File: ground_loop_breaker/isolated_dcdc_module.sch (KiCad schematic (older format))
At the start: 18 parts, among them J1 Conn_01x02_Male, J2 Conn_01x02_Male, J3 Conn_Coaxial

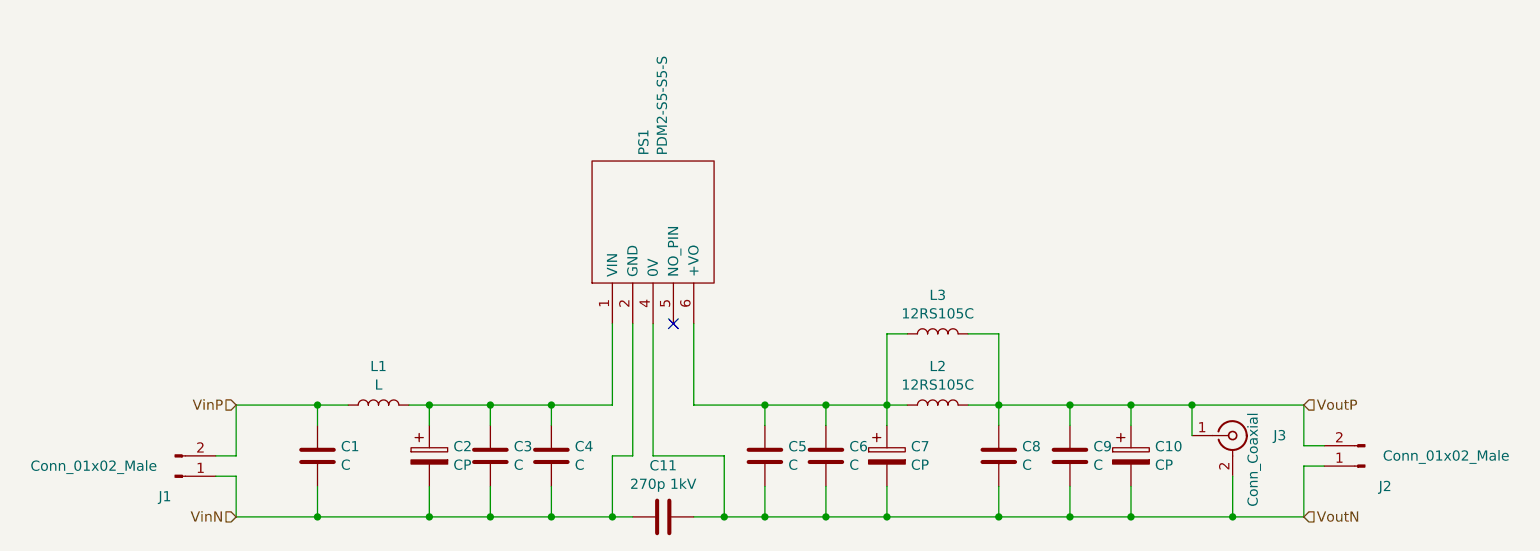
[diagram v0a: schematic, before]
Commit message: ground loop breaker fin
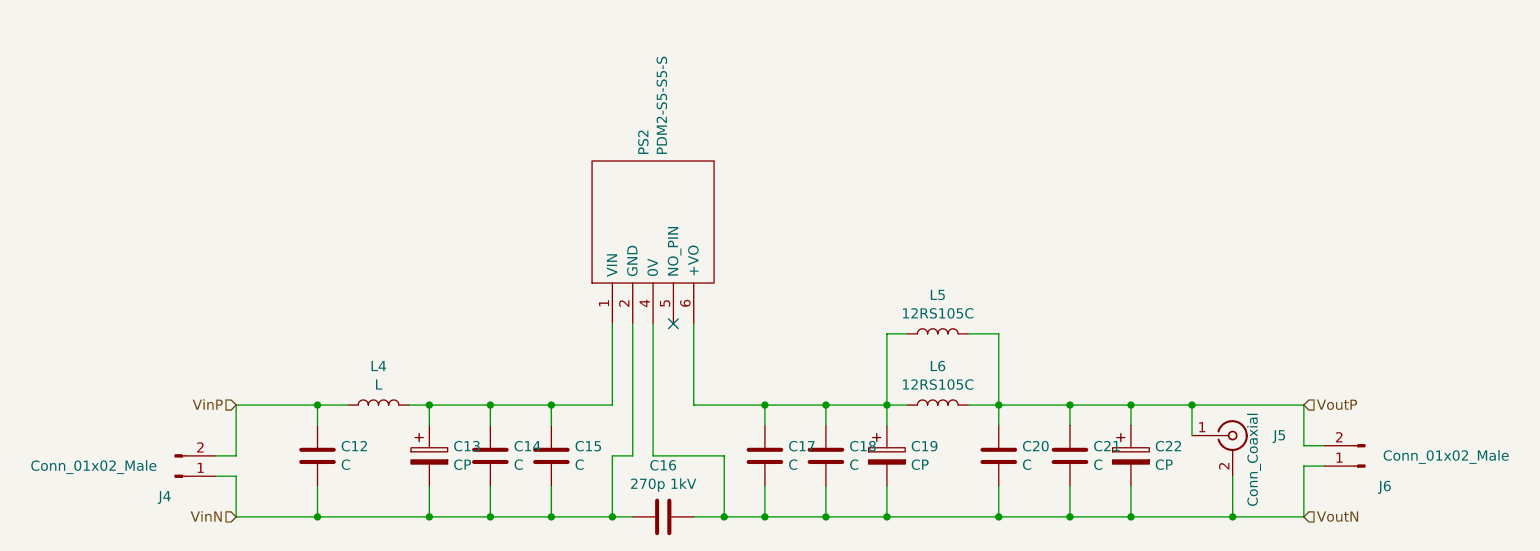
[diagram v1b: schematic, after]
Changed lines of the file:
@@
 $Descr A4 11693 8268
 encoding utf-8
-Sheet 2 5
+Sheet 4 5
 Title ""
 Date ""
@@
 AR Path="/613586DE/6135B5DE" Ref="C15"  Part="1"
 AR Path="/61358712/6135B5DE" Ref="C37"  Part="1"
-F 0 "C4" H 4165 3446 50  0000 L CNN
+F 0 "C15" H 4165 3446 50  0000 L CNN
 F 1 "C" H 4165 3355 50  0000 L CNN
 F 2 "SamacSys_Parts:C_1206_0805_dual" H 4088 3250 50  0001 C CNN
@@
 AR Path="/613586DE/6135B5E4" Ref="C14"  Part="1"
 AR Path="/61358712/6135B5E4" Ref="C36"  Part="1"
-F 0 "C3" H 3865 3446 50  0000 L CNN
+F 0 "C14" H 3865 3446 50  0000 L CNN
 F 1 "C" H 3865 3355 50  0000 L CNN
 F 2 "Capacitor_SMD:C_1206_3216Metric_Pad1.42x1.75mm_HandSolder" H 3788 3250 50  0001 C CNN
@@
 AR Path="/613586DE/6135B5F2" Ref="C13"  Part="1"
 AR Path="/61358712/6135B5F2" Ref="C35"  Part="1"
-F 0 "C2" H 3568 3446 50  0000 L CNN
+F 0 "C13" H 3568 3446 50  0000 L CNN
 F 1 "CP" H 3568 3355 50  0000 L CNN
 F 2 "SamacSys_Parts:CP_Radial_D8_P3.5_2.5" H 3488 3250 50  0001 C CNN
@@
 AR Path="/613586DE/6135B603" Ref="C12"  Part="1"
 AR Path="/61358712/6135B603" Ref="C34"  Part="1"
-F 0 "C1" H 3015 3446 50  0000 L CNN
+F 0 "C12" H 3015 3446 50  0000 L CNN
 F 1 "C" H 3015 3355 50  0000 L CNN
 F 2 "Capacitor_SMD:C_1206_3216Metric_Pad1.42x1.75mm_HandSolder" H 2938 3250 50  0001 C CNN
@@
 AR Path="/613586DE/6135B609" Ref="L4"  Part="1"
 AR Path="/61358712/6135B609" Ref="L10"  Part="1"
-F 0 "L1" V 3390 3150 50  0000 C CNN
+F 0 "L4" V 3390 3150 50  0000 C CNN
 F 1 "L" V 3299 3150 50  0000 C CNN
 F 2 "Inductor_SMD:L_Bourns-SRN4018" H 3200 3150 50  0001 C CNN
@@
 AR Path="/613586DE/61362EDF" Ref="C18"  Part="1"
 AR Path="/61358712/61362EDF" Ref="C40"  Part="1"
-F 0 "C6" H 5515 3446 50  0000 L CNN
+F 0 "C18" H 5515 3446 50  0000 L CNN
 F 1 "C" H 5515 3355 50  0000 L CNN
 F 2 "Capacitor_SMD:C_1206_3216Metric_Pad1.42x1.75mm_HandSolder" H 5438 3250 50  0001 C CNN
@@
 AR Path="/613586DE/61362EFB" Ref="C20"  Part="1"
 AR Path="/61358712/61362EFB" Ref="C42"  Part="1"
-F 0 "C8" H 6365 3446 50  0000 L CNN
+F 0 "C20" H 6365 3446 50  0000 L CNN
 F 1 "C" H 6365 3355 50  0000 L CNN
 F 2 "Capacitor_SMD:C_1206_3216Metric_Pad1.42x1.75mm_HandSolder" H 6288 3250 50  0001 C CNN
@@
 AR Path="/613586DE/61362F01" Ref="L6"  Part="1"
 AR Path="/61358712/61362F01" Ref="L12"  Part="1"
-F 0 "L2" V 6140 3150 50  0000 C CNN
+F 0 "L6" V 6140 3150 50  0000 C CNN
 F 1 "12RS105C" V 6049 3150 50  0000 C CNN
 F 2 "Inductor_THT:L_Radial_D10.5mm_P4.00x5.00mm_Murata_1200RS" H 5950 3150 50  0001 C CNN
@@
 AR Path="/613586DE/61365071" Ref="C17"  Part="1"
 AR Path="/61358712/61365071" Ref="C39"  Part="1"
-F 0 "C5" H 5215 3446 50  0000 L CNN
+F 0 "C17" H 5215 3446 50  0000 L CNN
 F 1 "C" H 5215 3355 50  0000 L CNN
 F 2 "SamacSys_Parts:C_1206_0805_dual" H 5138 3250 50  0001 C CNN
@@
 AR Path="/613586DE/613683EF" Ref="C21"  Part="1"
 AR Path="/61358712/613683EF" Ref="C43"  Part="1"
-F 0 "C9" H 6715 3446 50  0000 L CNN
+F 0 "C21" H 6715 3446 50  0000 L CNN
 F 1 "C" H 6715 3355 50  0000 L CNN
 F 2 "Capacitor_SMD:C_1206_3216Metric_Pad1.42x1.75mm_HandSolder" H 6638 3250 50  0001 C CNN
@@
 AR Path="/613586DE/613683F5" Ref="C22"  Part="1"
 AR Path="/61358712/613683F5" Ref="C44"  Part="1"
-F 0 "C10" H 7018 3446 50  0000 L CNN
+F 0 "C22" H 7018 3446 50  0000 L CNN
 F 1 "CP" H 7018 3355 50  0000 L CNN
 F 2 "SamacSys_Parts:CP_Radial_D10.0mm_P3.5_5" H 6938 3250 50  0001 C CNN
@@
 AR Path="/613586DE/6136C0C2" Ref="C19"  Part="1"
 AR Path="/61358712/6136C0C2" Ref="C41"  Part="1"
-F 0 "C7" H 5818 3446 50  0000 L CNN
+F 0 "C19" H 5818 3446 50  0000 L CNN
 F 1 "CP" H 5818 3355 50  0000 L CNN
 F 2 "SamacSys_Parts:CP_Radial_D8_P3.5_2.5" H 5738 3250 50  0001 C CNN
@@
 AR Path="/613586DE/6135AA09" Ref="J4"  Part="1"
 AR Path="/61358712/6135AA09" Ref="J10"  Part="1"
-F 0 "J1" H 2150 3600 50  0000 C CNN
+F 0 "J4" H 2150 3600 50  0000 C CNN
 F 1 "Conn_01x02_Male" H 1800 3450 50  0000 C CNN
 F 2 "Connector_PinHeader_2.54mm:PinHeader_1x02_P2.54mm_Vertical" H 2200 3500 50  0001 C CNN
@@
 AR Path="/613586DE/6135E9D7" Ref="J6"  Part="1"
 AR Path="/61358712/6135E9D7" Ref="J12"  Part="1"
-F 0 "J2" H 7950 3550 50  0000 C CNN
+F 0 "J6" H 7950 3550 50  0000 C CNN
 F 1 "Conn_01x02_Male" H 7650 3400 50  0000 C CNN
 F 2 "Connector_PinHeader_2.54mm:PinHeader_1x02_P2.54mm_Vertical" H 8050 3450 50  0001 C CNN
@@
 AR Path="/613586DE/613639F2" Ref="PS2"  Part="1"
 AR Path="/61358712/613639F2" Ref="PS4"  Part="1"
-F 0 "PS1" H 5178 2596 50  0000 L CNN
+F 0 "PS2" H 5178 2596 50  0000 L CNN
 F 1 "PDM2-S5-S5-S" H 5178 2505 50  0000 L CNN
 F 2 "PDM2S5S5S" H 5200 2850 50  0001 L CNN
@@
 AR Path="/613586DE/6137BF49" Ref="L5"  Part="1"
 AR Path="/61358712/6137BF49" Ref="L11"  Part="1"
-F 0 "L3" V 6140 2800 50  0000 C CNN
+F 0 "L5" V 6140 2800 50  0000 C CNN
 F 1 "12RS105C" V 6049 2800 50  0000 C CNN
 F 2 "Inductor_THT:L_Radial_D10.0mm_P5.00mm_Fastron_07P" H 5950 2800 50  0001 C CNN
@@
 AR Path="/613586DE/61387E06" Ref="C16"  Part="1"
 AR Path="/61358712/61387E06" Ref="C38"  Part="1"
-F 0 "C11" V 4348 3700 50  0000 C CNN
+F 0 "C16" V 4348 3700 50  0000 C CNN
 F 1 "270p 1kV" V 4439 3700 50  0000 C CNN
 F 2 "Capacitor_SMD:C_1206_3216Metric_Pad1.42x1.75mm_HandSolder" H 4638 3550 50  0001 C CNN
@@
 AR Path="/613586DE/61392101" Ref="J5"  Part="1"
 AR Path="/61358712/61392101" Ref="J11"  Part="1"
-F 0 "J3" H 7600 3300 50  0000 L CNN
+F 0 "J5" H 7600 3300 50  0000 L CNN
 F 1 "Conn_Coaxial" V 7500 2950 50  0000 L CNN
 F 2 "Connector_Coaxial:U.FL_Hirose_U.FL-R-SMT-1_Vertical" H 7400 3300 50  0001 C CNN

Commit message: Relay array board; Last checkup; Gerberfile updates
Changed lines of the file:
@@
 $Descr A4 11693 8268
 encoding utf-8
-Sheet 4 5
+Sheet 4 6
 Title ""
 Date ""
@@
 AR Path="/613586DE/6135B5DE" Ref="C15"  Part="1"
 AR Path="/61358712/6135B5DE" Ref="C37"  Part="1"
-F 0 "C15" H 4165 3446 50  0000 L CNN
+F 0 "C37" H 4165 3446 50  0000 L CNN
 F 1 "C" H 4165 3355 50  0000 L CNN
 F 2 "SamacSys_Parts:C_1206_0805_dual" H 4088 3250 50  0001 C CNN
@@
 AR Path="/613586DE/6135B5E4" Ref="C14"  Part="1"
 AR Path="/61358712/6135B5E4" Ref="C36"  Part="1"
-F 0 "C14" H 3865 3446 50  0000 L CNN
+F 0 "C36" H 3865 3446 50  0000 L CNN
 F 1 "C" H 3865 3355 50  0000 L CNN
 F 2 "Capacitor_SMD:C_1206_3216Metric_Pad1.42x1.75mm_HandSolder" H 3788 3250 50  0001 C CNN
@@
 AR Path="/613586DE/6135B5F2" Ref="C13"  Part="1"
 AR Path="/61358712/6135B5F2" Ref="C35"  Part="1"
-F 0 "C13" H 3568 3446 50  0000 L CNN
+F 0 "C35" H 3568 3446 50  0000 L CNN
 F 1 "CP" H 3568 3355 50  0000 L CNN
 F 2 "SamacSys_Parts:CP_Radial_D8_P3.5_2.5" H 3488 3250 50  0001 C CNN
@@
 AR Path="/613586DE/6135B603" Ref="C12"  Part="1"
 AR Path="/61358712/6135B603" Ref="C34"  Part="1"
-F 0 "C12" H 3015 3446 50  0000 L CNN
+F 0 "C34" H 3015 3446 50  0000 L CNN
 F 1 "C" H 3015 3355 50  0000 L CNN
 F 2 "Capacitor_SMD:C_1206_3216Metric_Pad1.42x1.75mm_HandSolder" H 2938 3250 50  0001 C CNN
@@
 AR Path="/613586DE/6135B609" Ref="L4"  Part="1"
 AR Path="/61358712/6135B609" Ref="L10"  Part="1"
-F 0 "L4" V 3390 3150 50  0000 C CNN
+F 0 "L10" V 3390 3150 50  0000 C CNN
 F 1 "L" V 3299 3150 50  0000 C CNN
 F 2 "Inductor_SMD:L_Bourns-SRN4018" H 3200 3150 50  0001 C CNN
@@
 AR Path="/613586DE/61362EDF" Ref="C18"  Part="1"
 AR Path="/61358712/61362EDF" Ref="C40"  Part="1"
-F 0 "C18" H 5515 3446 50  0000 L CNN
+F 0 "C40" H 5515 3446 50  0000 L CNN
 F 1 "C" H 5515 3355 50  0000 L CNN
 F 2 "Capacitor_SMD:C_1206_3216Metric_Pad1.42x1.75mm_HandSolder" H 5438 3250 50  0001 C CNN
@@
 AR Path="/613586DE/61362EFB" Ref="C20"  Part="1"
 AR Path="/61358712/61362EFB" Ref="C42"  Part="1"
-F 0 "C20" H 6365 3446 50  0000 L CNN
+F 0 "C42" H 6365 3446 50  0000 L CNN
 F 1 "C" H 6365 3355 50  0000 L CNN
 F 2 "Capacitor_SMD:C_1206_3216Metric_Pad1.42x1.75mm_HandSolder" H 6288 3250 50  0001 C CNN
@@
 AR Path="/613586DE/61362F01" Ref="L6"  Part="1"
 AR Path="/61358712/61362F01" Ref="L12"  Part="1"
-F 0 "L6" V 6140 3150 50  0000 C CNN
+F 0 "L12" V 6140 3150 50  0000 C CNN
 F 1 "12RS105C" V 6049 3150 50  0000 C CNN
 F 2 "Inductor_THT:L_Radial_D10.5mm_P4.00x5.00mm_Murata_1200RS" H 5950 3150 50  0001 C CNN
@@
 AR Path="/613586DE/61365071" Ref="C17"  Part="1"
 AR Path="/61358712/61365071" Ref="C39"  Part="1"
-F 0 "C17" H 5215 3446 50  0000 L CNN
+F 0 "C39" H 5215 3446 50  0000 L CNN
 F 1 "C" H 5215 3355 50  0000 L CNN
 F 2 "SamacSys_Parts:C_1206_0805_dual" H 5138 3250 50  0001 C CNN
@@
 AR Path="/613586DE/613683EF" Ref="C21"  Part="1"
 AR Path="/61358712/613683EF" Ref="C43"  Part="1"
-F 0 "C21" H 6715 3446 50  0000 L CNN
+F 0 "C43" H 6715 3446 50  0000 L CNN
 F 1 "C" H 6715 3355 50  0000 L CNN
 F 2 "Capacitor_SMD:C_1206_3216Metric_Pad1.42x1.75mm_HandSolder" H 6638 3250 50  0001 C CNN
@@
 AR Path="/613586DE/613683F5" Ref="C22"  Part="1"
 AR Path="/61358712/613683F5" Ref="C44"  Part="1"
-F 0 "C22" H 7018 3446 50  0000 L CNN
+F 0 "C44" H 7018 3446 50  0000 L CNN
 F 1 "CP" H 7018 3355 50  0000 L CNN
 F 2 "SamacSys_Parts:CP_Radial_D10.0mm_P3.5_5" H 6938 3250 50  0001 C CNN
@@
 AR Path="/613586DE/6136C0C2" Ref="C19"  Part="1"
 AR Path="/61358712/6136C0C2" Ref="C41"  Part="1"
-F 0 "C19" H 5818 3446 50  0000 L CNN
+F 0 "C41" H 5818 3446 50  0000 L CNN
 F 1 "CP" H 5818 3355 50  0000 L CNN
 F 2 "SamacSys_Parts:CP_Radial_D8_P3.5_2.5" H 5738 3250 50  0001 C CNN
@@
 AR Path="/613586DE/6135AA09" Ref="J4"  Part="1"
 AR Path="/61358712/6135AA09" Ref="J10"  Part="1"
-F 0 "J4" H 2150 3600 50  0000 C CNN
+F 0 "J10" H 2150 3600 50  0000 C CNN
 F 1 "Conn_01x02_Male" H 1800 3450 50  0000 C CNN
 F 2 "Connector_PinHeader_2.54mm:PinHeader_1x02_P2.54mm_Vertical" H 2200 3500 50  0001 C CNN
@@
 AR Path="/613586DE/6135E9D7" Ref="J6"  Part="1"
 AR Path="/61358712/6135E9D7" Ref="J12"  Part="1"
-F 0 "J6" H 7950 3550 50  0000 C CNN
+F 0 "J12" H 7950 3550 50  0000 C CNN
 F 1 "Conn_01x02_Male" H 7650 3400 50  0000 C CNN
 F 2 "Connector_PinHeader_2.54mm:PinHeader_1x02_P2.54mm_Vertical" H 8050 3450 50  0001 C CNN
@@
 AR Path="/613586DE/613639F2" Ref="PS2"  Part="1"
 AR Path="/61358712/613639F2" Ref="PS4"  Part="1"
-F 0 "PS2" H 5178 2596 50  0000 L CNN
+F 0 "PS4" H 5178 2596 50  0000 L CNN
 F 1 "PDM2-S5-S5-S" H 5178 2505 50  0000 L CNN
 F 2 "PDM2S5S5S" H 5200 2850 50  0001 L CNN
@@
 AR Path="/613586DE/6137BF49" Ref="L5"  Part="1"
 AR Path="/61358712/6137BF49" Ref="L11"  Part="1"
-F 0 "L5" V 6140 2800 50  0000 C CNN
+F 0 "L11" V 6140 2800 50  0000 C CNN
 F 1 "12RS105C" V 6049 2800 50  0000 C CNN
 F 2 "Inductor_THT:L_Radial_D10.0mm_P5.00mm_Fastron_07P" H 5950 2800 50  0001 C CNN
@@
 AR Path="/613586DE/61387E06" Ref="C16"  Part="1"
 AR Path="/61358712/61387E06" Ref="C38"  Part="1"
-F 0 "C16" V 4348 3700 50  0000 C CNN
+F 0 "C38" V 4348 3700 50  0000 C CNN
 F 1 "270p 1kV" V 4439 3700 50  0000 C CNN
 F 2 "Capacitor_SMD:C_1206_3216Metric_Pad1.42x1.75mm_HandSolder" H 4638 3550 50  0001 C CNN
@@
 AR Path="/613586DE/61392101" Ref="J5"  Part="1"
 AR Path="/61358712/61392101" Ref="J11"  Part="1"
-F 0 "J5" H 7600 3300 50  0000 L CNN
+F 0 "J11" H 7600 3300 50  0000 L CNN
 F 1 "Conn_Coaxial" V 7500 2950 50  0000 L CNN
 F 2 "Connector_Coaxial:U.FL_Hirose_U.FL-R-SMT-1_Vertical" H 7400 3300 50  0001 C CNN
